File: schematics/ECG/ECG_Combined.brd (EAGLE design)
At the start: 25.7 x 25.7 mm, 70 parts, among them IC1 ADS1293, IC2 LIS3DH, IC3 MCP1703, IC4 CC2541, IC5 FSA4157, IC6 FSA4157, IC7 FSA4157, X1 XTAL-2SMD, X2 XTAL_403, X3 XTAL-CSM7

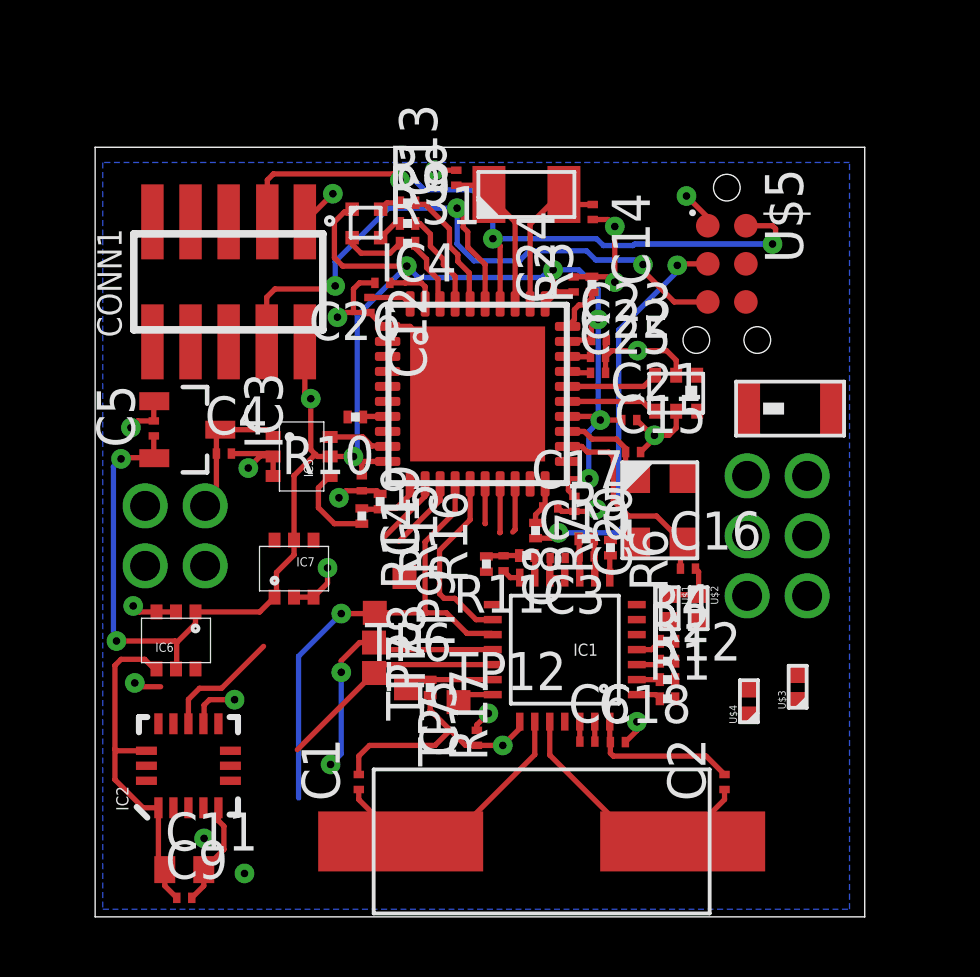
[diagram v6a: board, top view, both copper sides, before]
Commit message: board routed, still requires 50ohm ble antenna trace
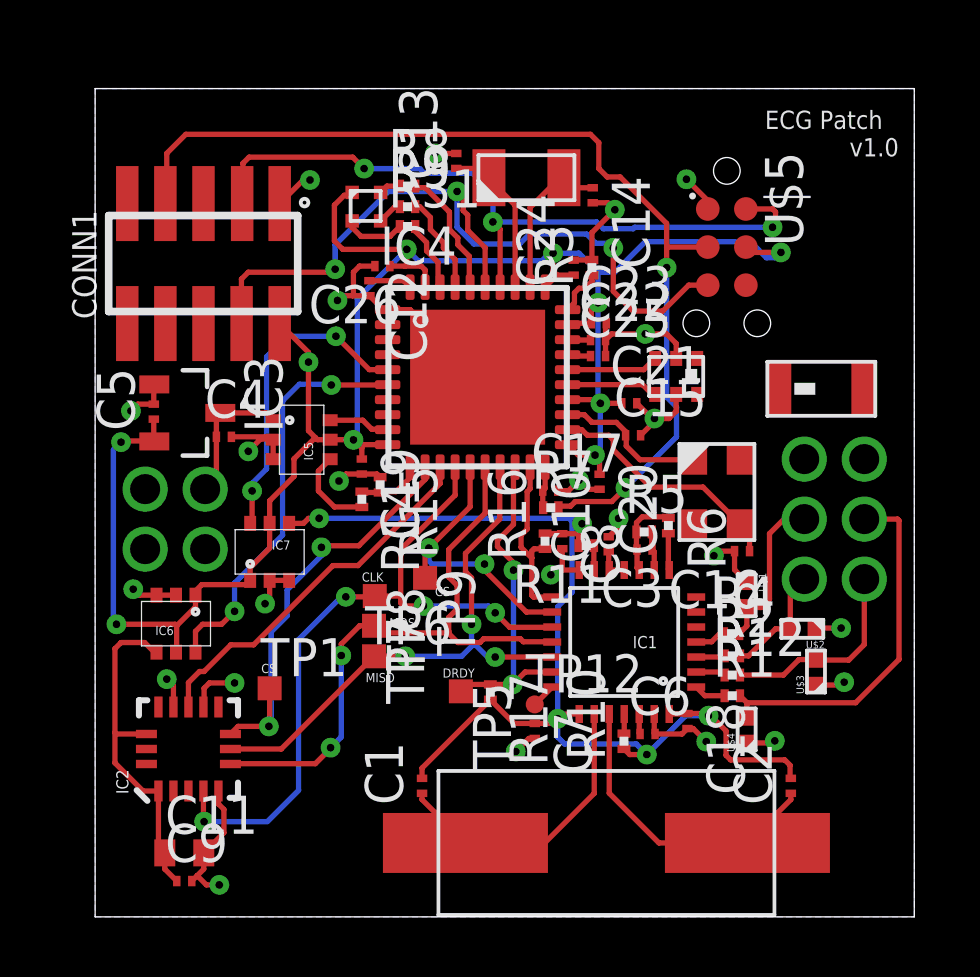
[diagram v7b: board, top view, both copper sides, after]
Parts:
- added TP1: TPSTP08SQ, testpad:TP08SQ
- TP12: value TPSTP08SQ -> TPSTP06R; device testpad:TP08SQ -> testpad:TP06R
- moved R10 14.0 mm to (17.6, 5.85), turned to 90 degrees
- moved U$2 3.52 mm to (23.6, 9.60), turned to 180 degrees
- moved U$1 2.60 mm to (21.7, 10.7)
- moved TP12 2.54 mm to (14.7, 7.08)
- moved C18 2.42 mm to (19.7, 6.53), turned to 270 degrees
- moved C2 2.21 mm to (23.2, 4.37)
- moved R2 2.17 mm to (21.2, 8.70)
- moved R12 2.16 mm to (21.2, 8.06)
- moved R1 2.16 mm to (21.2, 7.37)
- moved X3 2.16 mm to (17.0, 2.46)
- moved R4 2.15 mm to (21.2, 9.44)
- moved C1 2.11 mm to (10.9, 4.37)
- moved R16 2.10 mm to (15.0, 12.5)
- moved C8 2.09 mm to (15.6, 12.5)
- moved R6 2.07 mm to (19.1, 13.0)
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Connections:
- net ADS1293_RESET: no longer R10.1
- net ALARMB: now also IC4.19; no longer IC4.18
- net DRDYB: now also IC4.18; no longer IC4.19
- net ECG_VCC: now also R10.1
- net LA: now also CONN3.1; no longer CONN3.2
- net LL: now also CONN3.6; no longer CONN3.3
- net RA: now also CONN3.2; no longer CONN3.1
- net RL: now also CONN3.5; no longer CONN3.6
- net SPI_SS_ACCEL: now also TP1.TP
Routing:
- net ECG_VCC: track 14.7 -> 38.6 mm, vias 1 -> 5
- net RESET_N: track 13.7 -> 33.9 mm
- net ACCEL_VCC_SW: track 0.00 -> 13.7 mm, vias 0 -> 2
- net RA: track 0.00 -> 12.3 mm
- net SPI_SS_ACCEL: track 2.31 -> 14.2 mm, vias 0 -> 2
- net SPI_MOSI: track 10.3 -> 21.1 mm
- net ECG_VCC_SW: track 0.00 -> 10.6 mm, vias 0 -> 2
- net SPI_MISO: track 9.33 -> 18.8 mm, vias 0 -> 3
- net DRDYB: track 3.01 -> 11.0 mm, vias 0 -> 2
- net SPI_CLK: track 16.8 -> 24.5 mm, vias 2 -> 4
- net VCC: track 64.9 -> 72.5 mm, vias 9 -> 10
- net GND: track 43.8 -> 50.7 mm, vias 19 -> 24
- net LA: track 0.00 -> 6.76 mm
- net ACCEL_INT1: track 6.52 -> 12.5 mm
- net RL: track 0.00 -> 5.40 mm
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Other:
- board size 25.7 x 25.7 mm -> 27.3 x 27.6 mm
- board text added: "CLK"
- board text added: "CS"
- board text added: "DRDY"
- board text added: "ECG Patch"
- board text added: "MISO"
- board text added: "MOSI"
- board text added: "TO-DO: Calculate trace width for 50ohm impedence"
- board text added: "v1.0"

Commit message: adjusted board size. changed eeg pins
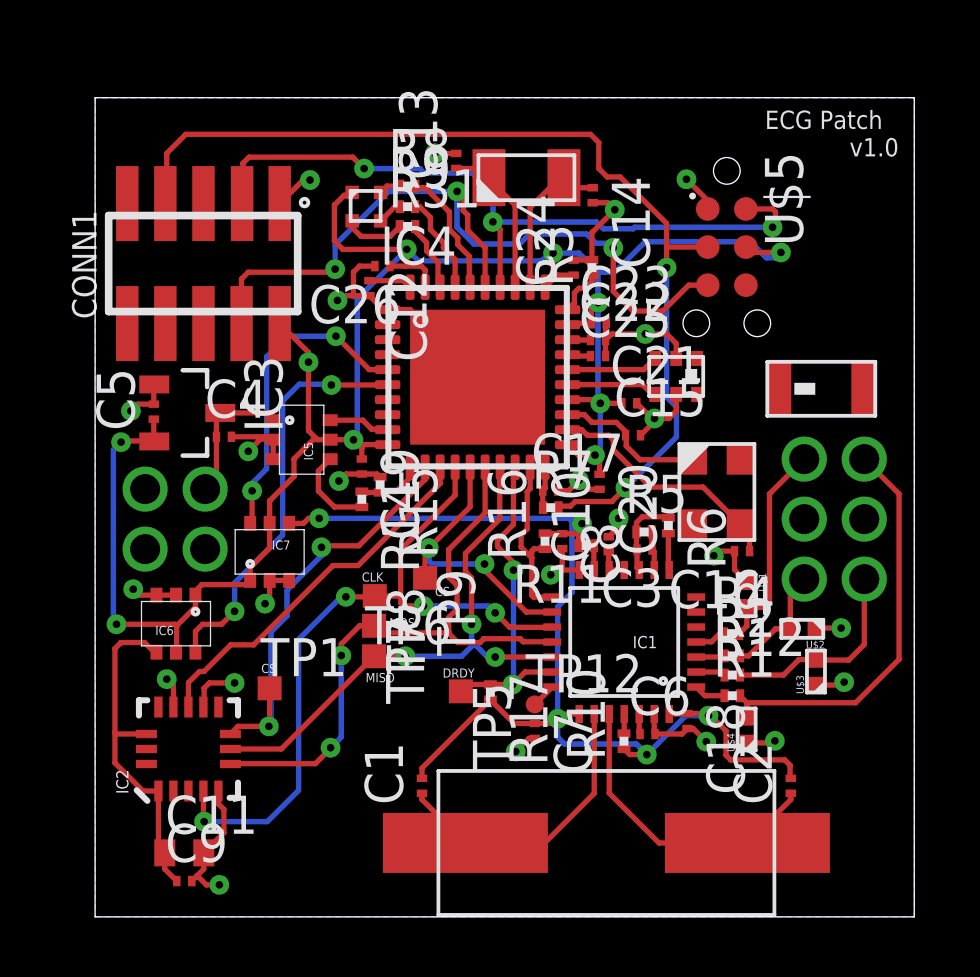
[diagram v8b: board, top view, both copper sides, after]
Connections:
- net RA: now also CONN3.3; no longer CONN3.2
- net RL: now also CONN3.4; no longer CONN3.5
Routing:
- net RL: track 5.40 -> 7.01 mm
- net RA: track 12.3 -> 13.6 mm
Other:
- board size 27.3 x 27.6 mm -> 27.3 x 27.3 mm
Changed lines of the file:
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@@
 <plain>
 <wire x1="0" y1="0" x2="27.305" y2="0" width="0" layer="20"/>
-<wire x1="27.305" y1="0" x2="27.305" y2="27.6098" width="0" layer="20"/>
-<wire x1="27.305" y1="27.6098" x2="0" y2="27.6098" width="0" layer="20"/>
-<wire x1="0" y1="27.6098" x2="0" y2="0" width="0" layer="20"/>
+<wire x1="27.305" y1="0" x2="27.305" y2="27.305" width="0" layer="20"/>
+<wire x1="27.305" y1="27.305" x2="0" y2="27.305" width="0" layer="20"/>
+<wire x1="0" y1="27.305" x2="0" y2="0" width="0" layer="20"/>
 <text x="22.3266" y="26.2636" size="0.6096" layer="21">ECG Patch</text>
 <text x="25.146" y="25.3492" size="0.6096" layer="21">v1.0</text>
@@
 <wire x1="17.2172" y1="19.431" x2="17.014" y2="19.2278" width="0.1778" layer="1"/>
 <polygon width="0.1778" layer="16">
-<vertex x="0" y="27.6098"/>
+<vertex x="0" y="27.305"/>
 <vertex x="0" y="0"/>
 <vertex x="27.305" y="0"/>
-<vertex x="27.305" y="27.6098"/>
+<vertex x="27.305" y="27.305"/>
 </polygon>
 <via x="11.3284" y="25.4508" extent="1-16" drill="0.254"/>
@@
 <wire x1="21.7242" y1="6.6548" x2="21.7242" y2="7.141" width="0.1778" layer="1"/>
 <wire x1="21.7242" y1="7.141" x2="21.494" y2="7.3712" width="0.1778" layer="1"/>
-<contactref element="CONN3" pad="2"/>
-<wire x1="25.638" y1="13.2588" x2="26.7462" y2="13.2588" width="0.1778" layer="1"/>
-<wire x1="26.7462" y1="13.2588" x2="26.797" y2="13.208" width="0.1778" layer="1"/>
-<wire x1="26.797" y1="13.208" x2="26.797" y2="8.5852" width="0.1778" layer="1"/>
+<wire x1="26.797" y1="14.0998" x2="26.797" y2="8.5852" width="0.1778" layer="1"/>
 <wire x1="26.797" y1="8.5852" x2="25.3492" y2="7.1374" width="0.1778" layer="1"/>
 <wire x1="25.3492" y1="7.1374" x2="21.7278" y2="7.1374" width="0.1778" layer="1"/>
 <wire x1="21.7278" y1="7.1374" x2="21.7242" y2="7.141" width="0.1778" layer="1"/>
+<contactref element="CONN3" pad="3"/>
+<wire x1="26.797" y1="14.0998" x2="25.638" y2="15.2588" width="0.1778" layer="1"/>
 </signal>
 <signal name="LL">
@@
 <contactref element="R4" pad="2"/>
 <contactref element="U$1" pad="2"/>
-<contactref element="CONN3" pad="5"/>
-<wire x1="23.638" y1="13.2588" x2="22.9616" y2="13.2588" width="0.1778" layer="1"/>
-<wire x1="22.9616" y1="13.2588" x2="22.479" y2="12.7762" width="0.1778" layer="1"/>
-<wire x1="22.479" y1="12.7762" x2="22.479" y2="10.5918" width="0.1778" layer="1"/>
+<wire x1="22.479" y1="14.0998" x2="22.479" y2="10.5918" width="0.1778" layer="1"/>
 <wire x1="22.479" y1="10.5918" x2="22.1996" y2="10.3124" width="0.1778" layer="1"/>
 <wire x1="22.1996" y1="10.3124" x2="21.7242" y2="10.3124" width="0.1778" layer="1"/>
@@
 <wire x1="21.7242" y1="10.3124" x2="21.7242" y2="9.6956" width="0.1778" layer="1"/>
 <wire x1="21.7242" y1="9.6956" x2="21.4686" y2="9.44" width="0.1778" layer="1"/>
+<contactref element="CONN3" pad="4"/>
+<wire x1="22.479" y1="14.0998" x2="23.638" y2="15.2588" width="0.1778" layer="1"/>
 </signal>
 <signal name="RLDOUT">
